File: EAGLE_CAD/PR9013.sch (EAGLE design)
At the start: 54 parts, among them J1 M3_SCREW_POST, SW1 SPST_TACT-KMR2, Y1 32.768kHz

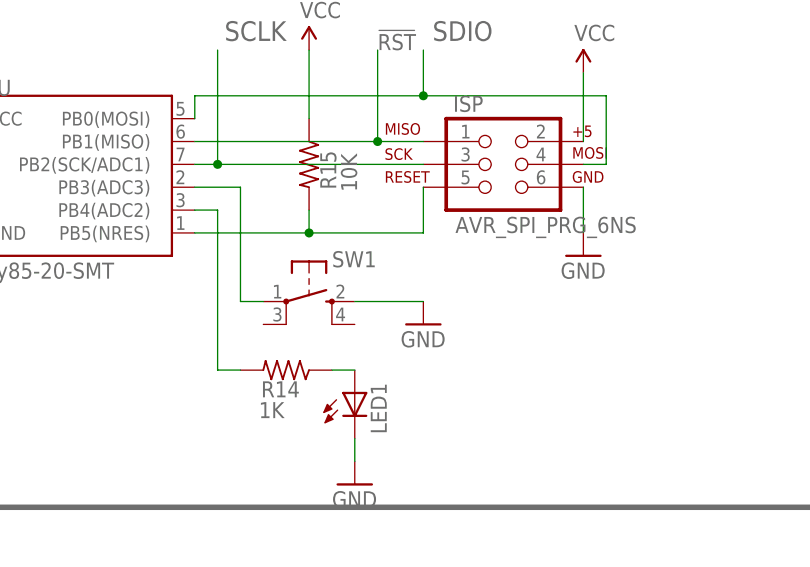
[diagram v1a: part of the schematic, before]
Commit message: Updated Parts
Added the C&K part to PR Parts Library and updated PR9013 to include
this part.
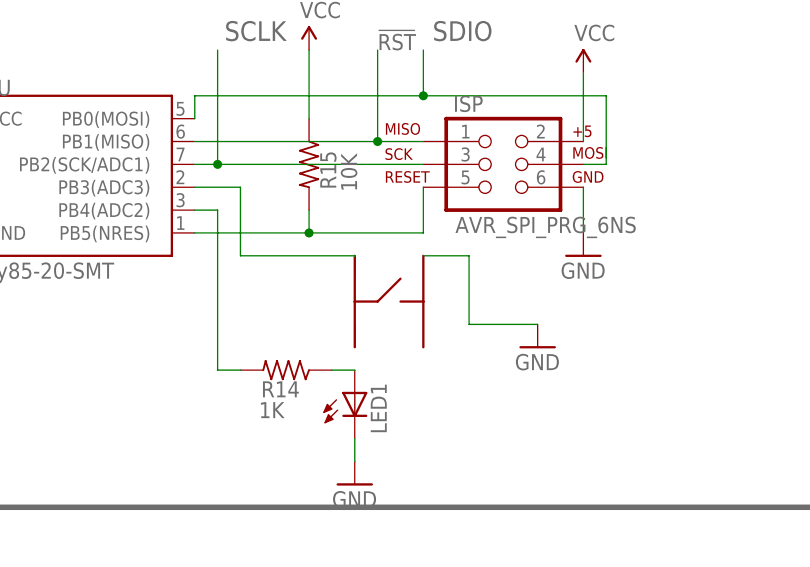
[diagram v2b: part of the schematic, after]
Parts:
- removed SW1: SPST_TACT-KMR2, adafruit:SPST_TACT-KMR2
- added U$1: C&KPTS6465, PR_Parts_Library:C&KPTS6465
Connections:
- net GND: now also U$1.P$1; no longer SW1.S
- net N$11: now also U$1.P$3; no longer SW1.P
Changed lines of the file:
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@@
 <part name="SUPPLY6" library="SparkFun-Aesthetics" deviceset="VCC" device=""/>
 <part name="SUPPLY7" library="SparkFun-Aesthetics" deviceset="VCC" device=""/>
-<part name="SW1" library="adafruit" deviceset="SPST_TACT" device="-KMR2"/>
 <part name="GND31" library="SparkFun" deviceset="GND" device=""/>
 <part name="ISP" library="SparkFun-Connectors" deviceset="AVR_SPI_PRG_6" device="NS"/>
@@
 <part name="C10" library="SparkFun-Passives" deviceset="CAP" device="0603-CAP"/>
 <part name="C11" library="SparkFun-Passives" deviceset="CAP" device="0603-CAP"/>
+<part name="U$1" library="PR_Parts_Library" deviceset="C&amp;KPTS6465" device=""/>
 </parts>
 <sheets>
@@
 <instance part="SUPPLY6" gate="1" x="129.54" y="139.7"/>
 <instance part="SUPPLY7" gate="1" x="139.7" y="139.7"/>
-<instance part="SW1" gate="G$1" x="200.66" y="111.76" smashed="yes" rot="R270">
-<attribute name="NAME" x="203.2" y="115.57" size="1.778" layer="95"/>
-</instance>
-<instance part="GND31" gate="1" x="213.36" y="109.22"/>
+<instance part="GND31" gate="1" x="226.06" y="106.68"/>
 <instance part="ISP" gate="G$1" x="220.98" y="127"/>
 <instance part="LED1" gate="G$1" x="205.74" y="101.6"/>
@@
 <instance part="C10" gate="G$1" x="81.28" y="66.04" rot="R90"/>
 <instance part="C11" gate="G$1" x="81.28" y="73.66" rot="R90"/>
+<instance part="U$1" gate="G$1" x="210.82" y="111.76" rot="R270"/>
 </instances>
 <busses>
@@
 </segment>
 <segment>
-<pinref part="SW1" gate="G$1" pin="S"/>
 <pinref part="GND31" gate="1" pin="GND"/>
-<wire x1="213.36" y1="111.76" x2="205.74" y2="111.76" width="0.1524" layer="91"/>
+<wire x1="226.06" y1="109.22" x2="218.44" y2="109.22" width="0.1524" layer="91"/>
+<wire x1="218.44" y1="109.22" x2="218.44" y2="116.84" width="0.1524" layer="91"/>
+<pinref part="U$1" gate="G$1" pin="P$1"/>
+<wire x1="218.44" y1="116.84" x2="213.36" y2="116.84" width="0.1524" layer="91"/>
 </segment>
 <segment>
@@
 <net name="N$11" class="0">
 <segment>
-<wire x1="195.58" y1="111.76" x2="193.04" y2="111.76" width="0.1524" layer="91"/>
-<wire x1="193.04" y1="111.76" x2="193.04" y2="124.46" width="0.1524" layer="91"/>
+<wire x1="205.74" y1="116.84" x2="193.04" y2="116.84" width="0.1524" layer="91"/>
+<wire x1="193.04" y1="116.84" x2="193.04" y2="124.46" width="0.1524" layer="91"/>
 <pinref part="MCU" gate="G$1" pin="PB3(ADC3)"/>
 <wire x1="193.04" y1="124.46" x2="187.96" y2="124.46" width="0.1524" layer="91"/>
-<pinref part="SW1" gate="G$1" pin="P"/>
-</segment>
-</net>
+<pinref part="U$1" gate="G$1" pin="P$3"/>
+</segment>
+</net>

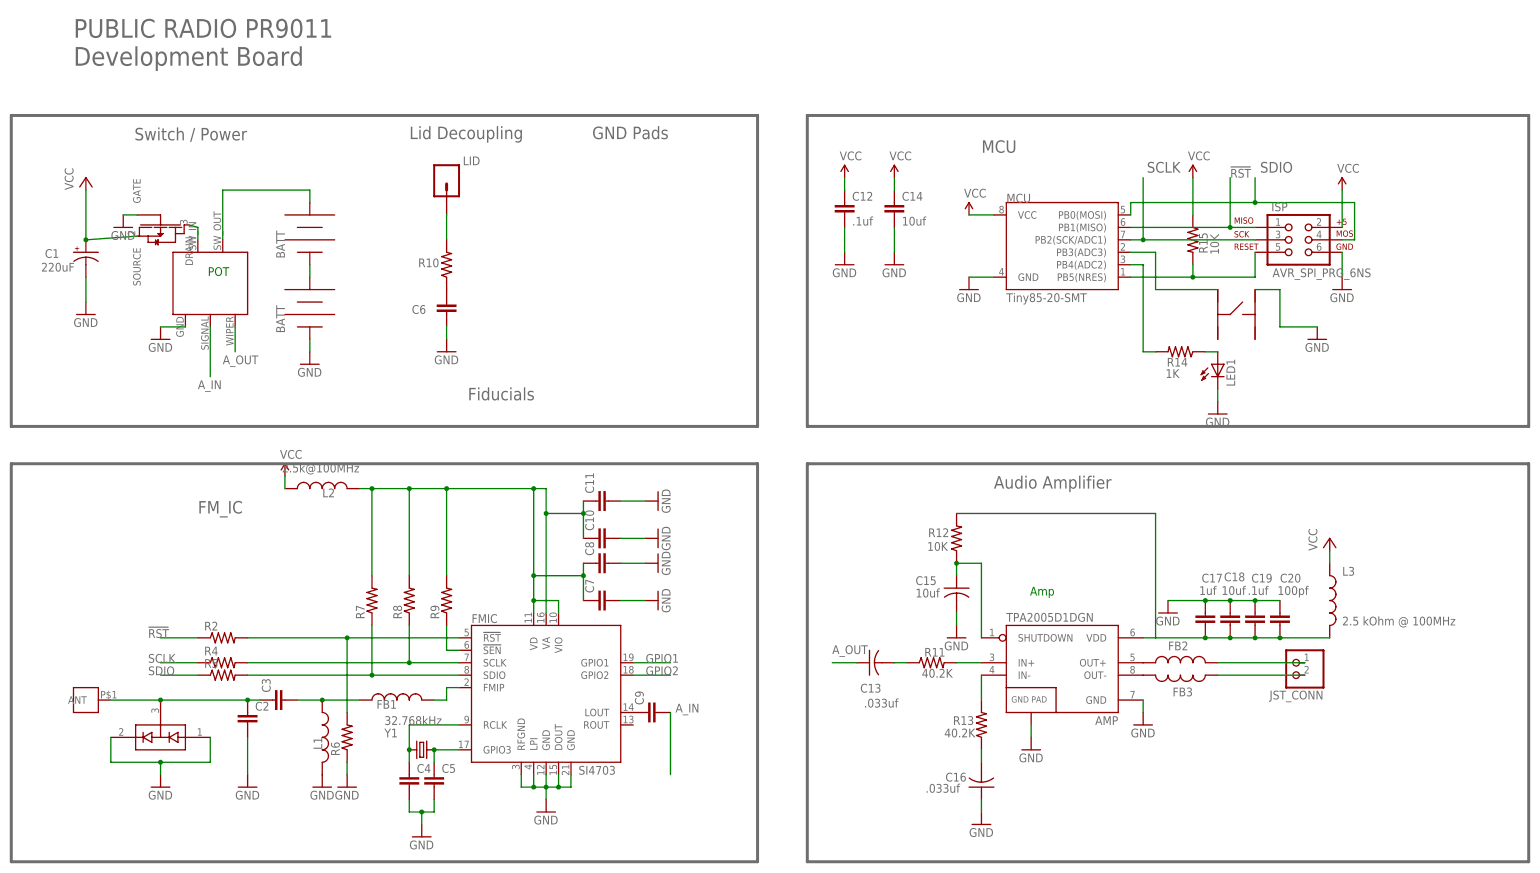
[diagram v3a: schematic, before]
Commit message: New Layout and Updated Packages
-Updated the package for:
  o Tactile Switch
  o Decoupling Cap, C1
  o Xtal

-Routed Amp, & MCU.

Note:
Alternative Xtal package is in the PR_Parts_Lib
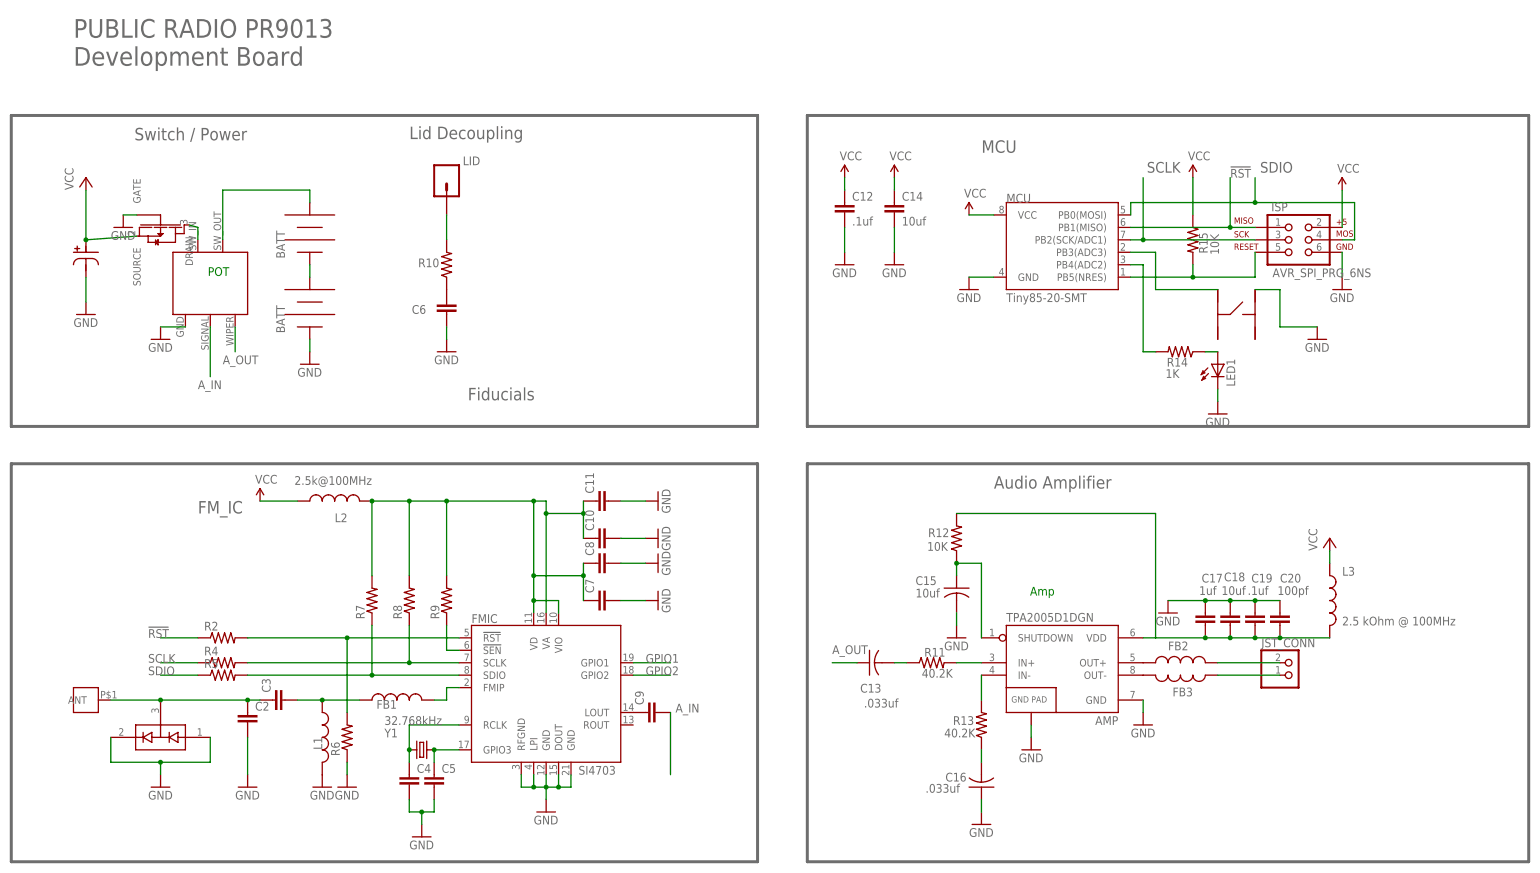
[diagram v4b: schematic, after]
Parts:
- removed C1: 220uF, SparkFun-Passives:CAP_POLC
- added U$2: NICHICON_SERIESUD, PR_Parts_Library:NICHICON_SERIESUD
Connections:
- removed net OUT-: FB3.1, JST_CONN.1
- new net N$22: FB3.1, JST_CONN.2
- net GND: now also U$2.P$2; no longer C1.-
- net N$9: now also JST_CONN.1; no longer JST_CONN.2
- net VCC: now also U$2.P$1; no longer C1.+
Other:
- note added: "PUBLIC RADIO PR9013 Development Board"
- note removed: "GND Pads"
- note removed: "PUBLIC RADIO PR9011 Development Board"
- moved on the sheet: JST_CONN, L2
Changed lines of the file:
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@@
 <setting verticaltext="up"/>
 </settings>
-<grid distance="0.1" unitdist="inch" unit="inch" style="lines" multiple="1" display="no" altdistance="0.01" altunitdist="inch" altunit="inch"/>
+<grid distance="0.1" unitdist="inch" unit="inch" style="lines" multiple="1" display="yes" altdistance="0.01" altunitdist="inch" altunit="inch"/>
 <layers>
 <layer number="1" name="Top" color="4" fill="1" visible="no" active="no"/>
@@
 <part name="C20" library="SparkFun-Passives" deviceset="CAP" device="0805" value="100pf"/>
 <part name="LID" library="SparkFun-Connectors" deviceset="M01" device="PTH"/>
-<part name="C1" library="SparkFun-Passives" deviceset="CAP_POL" device="C" value="220uF"/>
 <part name="C6" library="SparkFun-Passives" deviceset="CAP" device="0805"/>
 <part name="R10" library="SparkFun-Passives" deviceset="RESISTOR" device="0805-RES"/>
@@
 <part name="C11" library="SparkFun-Passives" deviceset="CAP" device="0603-CAP"/>
 <part name="U$1" library="PR_Parts_Library" deviceset="C&amp;KPTS6465" device=""/>
+<part name="U$2" library="PR_Parts_Library" deviceset="NICHICON_SERIESUD" device=""/>
 </parts>
 <sheets>
@@
 <text x="160.02" y="76.2" size="2.54" layer="96">Audio Amplifier </text>
 <text x="157.48" y="144.78" size="2.54" layer="96">MCU</text>
-<text x="-27.94" y="162.56" size="3.81" layer="96">PUBLIC RADIO PR9011
+<text x="-27.94" y="162.56" size="3.81" layer="96">PUBLIC RADIO PR9013
 Development Board </text>
-<text x="77.978" y="147.574" size="2.54" layer="96">GND Pads </text>
 <text x="52.578" y="94.234" size="2.54" layer="96">Fiducials </text>
 </plain>
@@
 <instance part="GND20" gate="1" x="91.44" y="66.04" rot="R90"/>
 <instance part="GND9" gate="1" x="27.94" y="15.24"/>
-<instance part="SUPPLY5" gate="1" x="15.24" y="78.74"/>
+<instance part="SUPPLY5" gate="1" x="10.16" y="73.66"/>
 <instance part="AMP" gate="G$1" x="172.72" y="40.64"/>
 <instance part="GND27" gate="1" x="167.64" y="22.86"/>
@@
 <instance part="GND28" gate="1" x="190.5" y="27.94"/>
 <instance part="GND7" gate="1" x="22.86" y="15.24"/>
-<instance part="L2" gate="G$1" x="22.86" y="76.2" smashed="yes" rot="R90">
-<attribute name="NAME" x="22.86" y="74.422" size="1.778" layer="95"/>
-<attribute name="VALUE" x="30.48" y="81.28" size="1.778" layer="96" rot="R180"/>
+<instance part="L2" gate="G$1" x="25.4" y="73.66" smashed="yes" rot="R90">
+<attribute name="NAME" x="25.4" y="69.342" size="1.778" layer="95"/>
+<attribute name="VALUE" x="33.02" y="78.74" size="1.778" layer="96" rot="R180"/>
 </instance>
 <instance part="L3" gate="G$1" x="228.6" y="53.34"/>
@@
 <attribute name="NAME" x="51.562" y="142.24" size="1.778" layer="95"/>
 </instance>
-<instance part="C1" gate="G$1" x="-25.4" y="124.46" smashed="yes">
-<attribute name="NAME" x="-33.782" y="123.317" size="1.778" layer="95"/>
-<attribute name="VALUE" x="-34.544" y="120.523" size="1.778" layer="96"/>
-</instance>
 <instance part="C6" gate="G$1" x="48.26" y="111.76" smashed="yes">
 <attribute name="NAME" x="41.148" y="111.887" size="1.778" layer="95"/>
@@
 </instance>
 <instance part="SUPPLY1" gate="1" x="200.66" y="139.7"/>
-<instance part="JST_CONN" gate="G$1" x="220.98" y="40.64" rot="R180"/>
+<instance part="JST_CONN" gate="G$1" x="220.98" y="38.1"/>
 <instance part="C2" gate="G$1" x="7.62" y="27.94"/>
 <instance part="C3" gate="G$1" x="15.24" y="33.02" rot="R90"/>
@@
 <instance part="C11" gate="G$1" x="81.28" y="73.66" rot="R90"/>
 <instance part="U$1" gate="G$1" x="210.82" y="111.76" rot="R270"/>
+<instance part="U$2" gate="G$1" x="-25.4" y="124.46"/>
 </instances>
 <busses>
@@
 </segment>
 <segment>
-<pinref part="GND2" gate="1" pin="GND"/>
-<wire x1="-25.4" y1="114.3" x2="-25.4" y2="119.38" width="0.1524" layer="91"/>
-<pinref part="C1" gate="G$1" pin="-"/>
-</segment>
-<segment>
 <pinref part="GND12" gate="1" pin="GND"/>
 <wire x1="48.26" y1="106.68" x2="48.26" y2="109.22" width="0.1524" layer="91"/>
@@
 <wire x1="0" y1="20.32" x2="-10.16" y2="20.32" width="0.1524" layer="91"/>
 <junction x="-10.16" y="20.32"/>
+</segment>
+<segment>
+<pinref part="GND2" gate="1" pin="GND"/>
+<pinref part="U$2" gate="G$1" pin="P$2"/>
+<wire x1="-25.4" y1="114.3" x2="-25.4" y2="119.38" width="0.1524" layer="91"/>
 </segment>
 </net>
@@
 <net name="3.3V" class="0">
 <segment>
-<wire x1="33.02" y1="58.42" x2="33.02" y2="76.2" width="0.1524" layer="91"/>
+<wire x1="33.02" y1="58.42" x2="33.02" y2="73.66" width="0.1524" layer="91"/>
 <wire x1="76.2" y1="60.96" x2="76.2" y2="58.42" width="0.1524" layer="91"/>
 <pinref part="FMIC" gate="G$1" pin="VIO"/>
@@
 <wire x1="68.58" y1="71.12" x2="68.58" y2="50.8" width="0.1524" layer="91"/>
 <junction x="76.2" y="71.12"/>
-<wire x1="68.58" y1="71.12" x2="68.58" y2="76.2" width="0.1524" layer="91"/>
+<wire x1="68.58" y1="71.12" x2="68.58" y2="73.66" width="0.1524" layer="91"/>
 <junction x="68.58" y="71.12"/>
 <pinref part="L2" gate="G$1" pin="2"/>
-<wire x1="68.58" y1="76.2" x2="66.04" y2="76.2" width="0.1524" layer="91"/>
-<wire x1="66.04" y1="76.2" x2="48.26" y2="76.2" width="0.1524" layer="91"/>
-<wire x1="48.26" y1="76.2" x2="40.64" y2="76.2" width="0.1524" layer="91"/>
-<wire x1="40.64" y1="76.2" x2="33.02" y2="76.2" width="0.1524" layer="91"/>
-<wire x1="33.02" y1="76.2" x2="30.48" y2="76.2" width="0.1524" layer="91"/>
-<wire x1="66.04" y1="58.42" x2="66.04" y2="76.2" width="0.1524" layer="91"/>
+<wire x1="68.58" y1="73.66" x2="66.04" y2="73.66" width="0.1524" layer="91"/>
+<wire x1="66.04" y1="73.66" x2="48.26" y2="73.66" width="0.1524" layer="91"/>
+<wire x1="48.26" y1="73.66" x2="40.64" y2="73.66" width="0.1524" layer="91"/>
+<wire x1="40.64" y1="73.66" x2="33.02" y2="73.66" width="0.1524" layer="91"/>
+<wire x1="66.04" y1="58.42" x2="66.04" y2="73.66" width="0.1524" layer="91"/>
 <junction x="66.04" y="58.42"/>
-<junction x="66.04" y="76.2"/>
-<wire x1="48.26" y1="58.42" x2="48.26" y2="76.2" width="0.1524" layer="91"/>
-<junction x="48.26" y="76.2"/>
-<wire x1="40.64" y1="58.42" x2="40.64" y2="76.2" width="0.1524" layer="91"/>
-<junction x="40.64" y="76.2"/>
-<junction x="33.02" y="76.2"/>
+<junction x="66.04" y="73.66"/>
+<wire x1="48.26" y1="58.42" x2="48.26" y2="73.66" width="0.1524" layer="91"/>
+<junction x="48.26" y="73.66"/>
+<wire x1="40.64" y1="58.42" x2="40.64" y2="73.66" width="0.1524" layer="91"/>
+<junction x="40.64" y="73.66"/>
+<junction x="33.02" y="73.66"/>
 <pinref part="C7" gate="G$1" pin="1"/>
 <pinref part="C8" gate="G$1" pin="1"/>
@@
 <wire x1="-14.986" y1="127.762" x2="-25.4" y2="127" width="0.1524" layer="91"/>
 <wire x1="-25.4" y1="127" x2="-25.4" y2="137.16" width="0.1524" layer="91"/>
-<pinref part="C1" gate="G$1" pin="+"/>
+<pinref part="U$2" gate="G$1" pin="P$1"/>
 <junction x="-25.4" y="127"/>
 </segment>
@@
 <pinref part="L2" gate="G$1" pin="1"/>
 <pinref part="SUPPLY5" gate="1" pin="VCC"/>
-<wire x1="15.24" y1="78.74" x2="15.24" y2="76.2" width="0.1524" layer="91"/>
+<wire x1="17.78" y1="73.66" x2="10.16" y2="73.66" width="0.1524" layer="91"/>
 </segment>
 <segment>
@@
 </segment>
 </net>
-<net name="OUT-" class="0">
-<segment>
-<pinref part="FB3" gate="G$1" pin="1"/>
-<pinref part="JST_CONN" gate="G$1" pin="1"/>
-<wire x1="223.52" y1="38.1" x2="205.74" y2="38.1" width="0.1524" layer="91"/>
-</segment>
-</net>
 <net name="N$34" class="0">
 <segment>
@@
 </segment>
 </net>
-<net name="N$9" class="0">
-<segment>
-<pinref part="FB2" gate="G$1" pin="2"/>
-<pinref part="JST_CONN" gate="G$1" pin="2"/>
-<wire x1="205.74" y1="40.64" x2="223.52" y2="40.64" width="0.1524" layer="91"/>
-</segment>
-</net>
 <net name="N$10" class="0">
 <segment>
@@
 </segment>
 </net>
+<net name="N$9" class="0">
+<segment>
+<pinref part="FB2" gate="G$1" pin="2"/>
+<pinref part="JST_CONN" gate="G$1" pin="1"/>
+<wire x1="205.74" y1="40.64" x2="218.44" y2="40.64" width="0.1524" layer="91"/>
+</segment>
+</net>
+<net name="N$22" class="0">
+<segment>
+<pinref part="JST_CONN" gate="G$1" pin="2"/>
+<pinref part="FB3" gate="G$1" pin="1"/>
+<wire x1="218.44" y1="38.1" x2="205.74" y2="38.1" width="0.1524" layer="91"/>
+</segment>
+</net>
